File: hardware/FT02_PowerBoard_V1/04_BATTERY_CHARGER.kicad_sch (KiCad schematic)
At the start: 0 parts

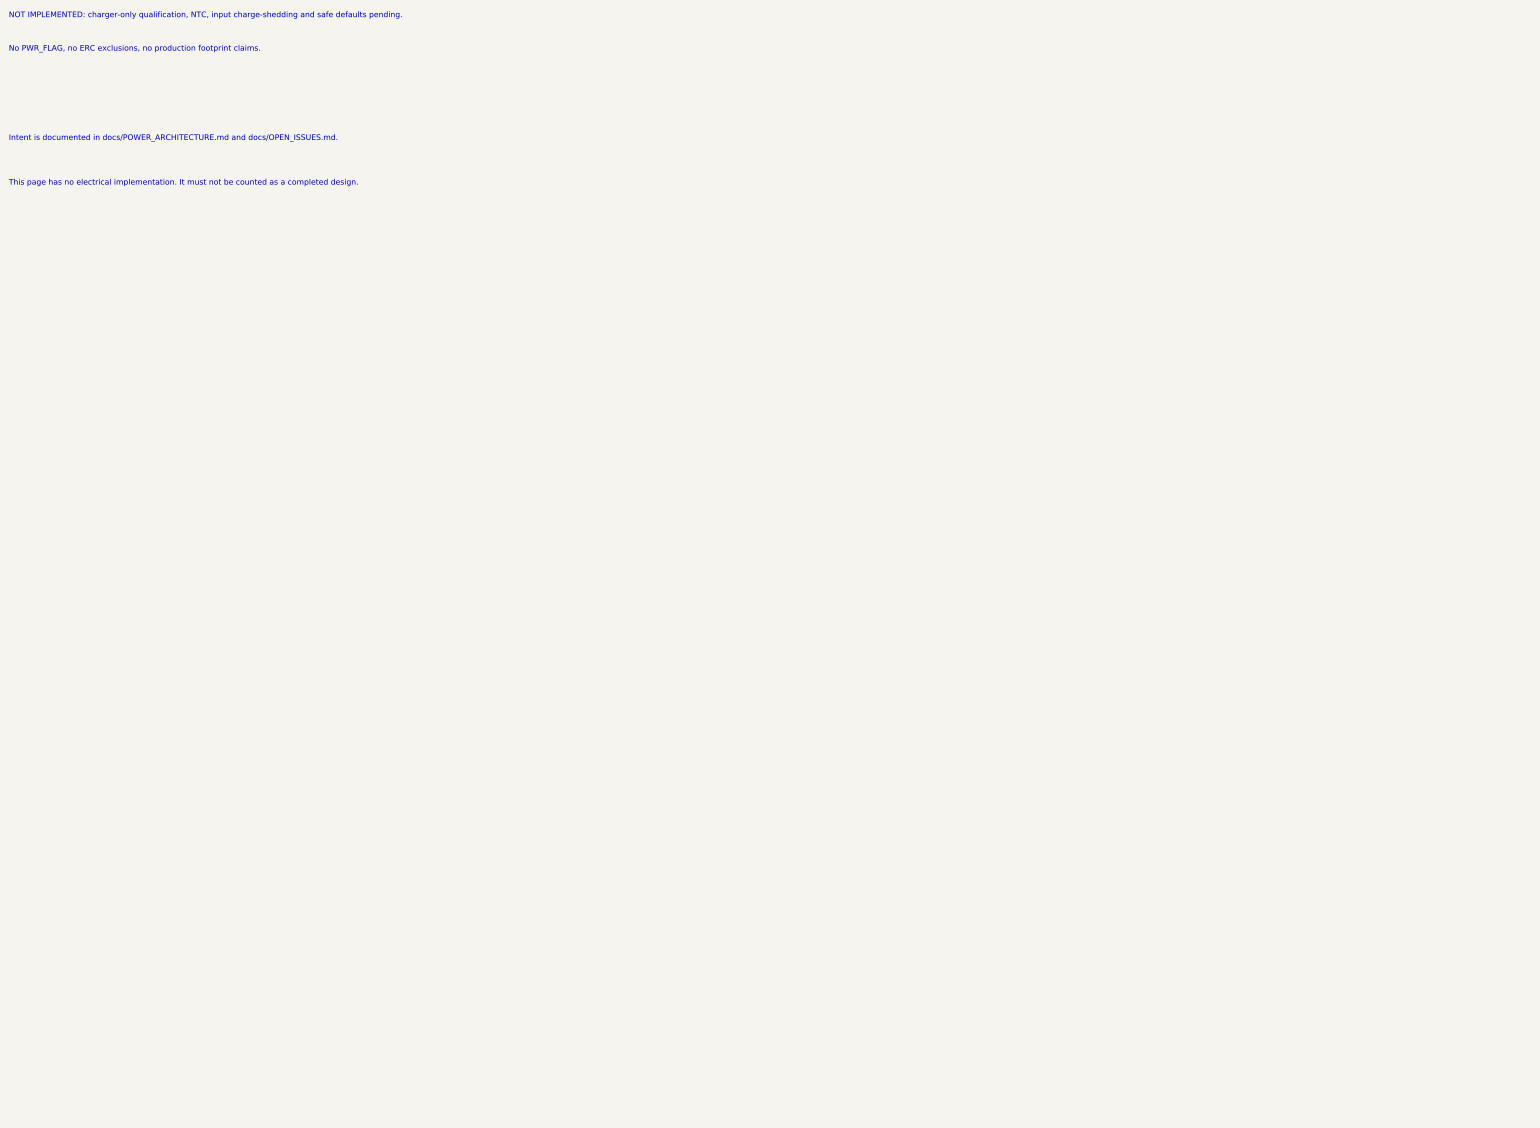
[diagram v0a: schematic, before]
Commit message: Wire FT02 Phase 1 power stages and verify partial shunt boundary
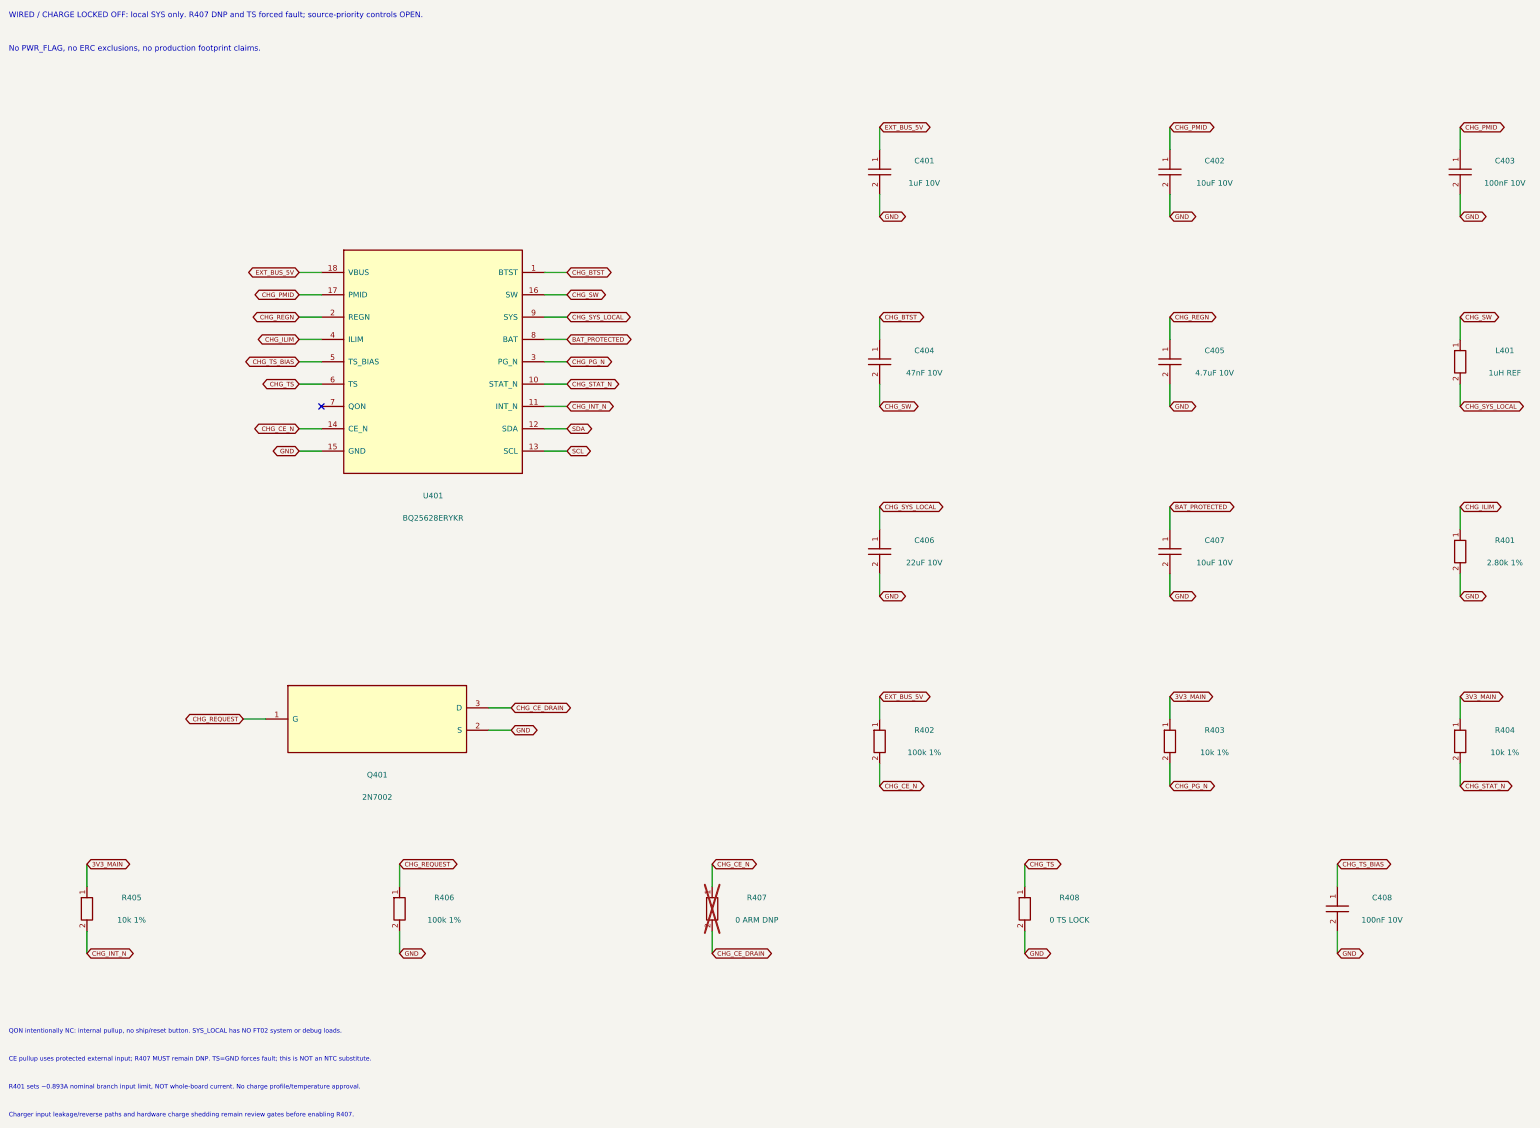
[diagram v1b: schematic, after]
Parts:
- added C401: 1uF 10V, symbol FT02_Reference:C
- added C402, C407: 10uF 10V, symbol FT02_Reference:C
- added C403, C408: 100nF 10V, symbol FT02_Reference:C
- added C404: 47nF 10V, symbol FT02_Reference:C
- added C405: 4.7uF 10V, symbol FT02_Reference:C
- added C406: 22uF 10V, symbol FT02_Reference:C
- added L401: 1uH REF, symbol FT02_Reference:L
- added Q401: 2N7002, symbol FT02_Reference:2N7002
- added R401: 2.80k 1%, symbol FT02_Reference:R
- added R402, R406: 100k 1%, symbol FT02_Reference:R
- added R403, R404, R405: 10k 1%, symbol FT02_Reference:R
- added R407: 0 ARM DNP, symbol FT02_Reference:R
- added R408: 0 TS LOCK, symbol FT02_Reference:R
- added U401: BQ25628ERYKR, symbol FT02_Reference:BQ25628E
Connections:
- new net 3V3_MAIN: R403.1, R404.1, R405.1
- new net BAT_PROTECTED: C407.1, U401.8 (BAT)
- new net CHG_BTST: C404.1, U401.1 (BTST)
- new net CHG_CE_DRAIN: Q401.3 (D), R407.2
- new net CHG_CE_N: R402.2, R407.1, U401.14 (CE_N)
- new net CHG_ILIM: R401.1, U401.4 (ILIM)
- new net CHG_INT_N: R405.2, U401.11 (INT_N)
- new net CHG_PG_N: R403.2, U401.3 (PG_N)
- new net CHG_PMID: C402.1, C403.1, U401.17 (PMID)
- new net CHG_REGN: C405.1, U401.2 (REGN)
- new net CHG_REQUEST: Q401.1 (G), R406.1
- new net CHG_STAT_N: R404.2, U401.10 (STAT_N)
- new net CHG_SW: C404.2, L401.1, U401.16 (SW)
- new net CHG_SYS_LOCAL: C406.1, L401.2, U401.9 (SYS)
- new net CHG_TS: R408.1, U401.6 (TS)
- new net CHG_TS_BIAS: C408.1, U401.5 (TS_BIAS)
- new net EXT_BUS_5V: C401.1, R402.1, U401.18 (VBUS)
- new net GND: C401.2, C402.2, C403.2, C405.2, C406.2, C407.2, C408.2, Q401.2 (S), R401.2, R406.2, R408.2, U401.15 (GND)
- new net SCL: U401.13 (SCL)
- new net SDA: U401.12 (SDA)
- no-connect marks 0 -> 1
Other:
- note added: "CE pullup uses protected external input; R407 MUST remain DNP. TS=GND forces fault; this is NOT an NTC substitute."
- note added: "Charger input leakage/reverse paths and hardware charge shedding remain review gates before enabling R407."
- note added: "QON intentionally NC: internal pullup, no ship/reset button. SYS_LOCAL has NO FT02 system or debug loads."
- note added: "R401 sets ~0.893A nominal branch input limit, NOT whole-board current. No charge profile/temperature approval."
- note added: "WIRED / CHARGE LOCKED OFF: local SYS only. R407 DNP and TS forced fault; source-priority controls OPEN."
- note removed: "Intent is documented in docs/POWER_ARCHITECTURE.md and docs/OPEN_ISSUES.md."
- note removed: "NOT IMPLEMENTED: charger-only qualification, NTC, input charge-shedding and safe defaults pending."
- note removed: "This page has no electrical implementation. It must not be counted as a completed design."
